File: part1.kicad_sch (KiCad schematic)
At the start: 20 parts, among them U1 74LS377, U10 Am2918, U11 Am2919, U12 Am2919, U13 74LS139, U14 74LS399, U15 74LS175, U16 Am2921, U17 Am2921, U18 Am27S19, U19 Am27S19, U2 Am2919, U3 Am2919, U4 Am27S21, U5 Am27S21, U6 Am27S21, U7 Am2910, U8 Am2918, U9 Am2918

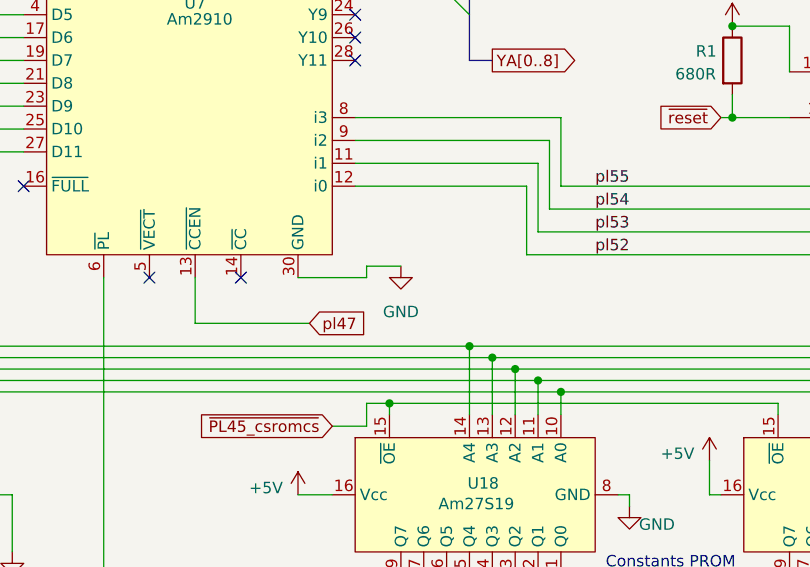
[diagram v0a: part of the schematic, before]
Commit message: Start with ALU sheet
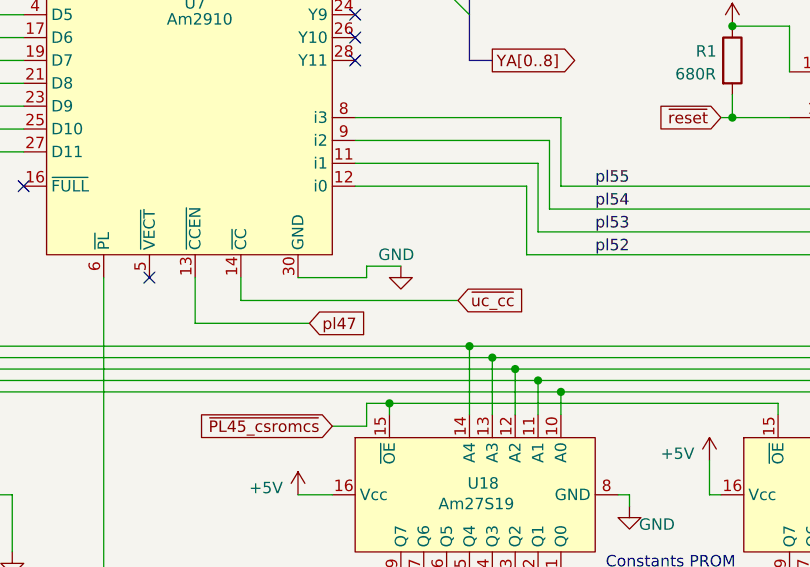
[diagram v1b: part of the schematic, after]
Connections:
- net ~{uc_cc}: now reaches U7.14 (~{CC})
- no-connect marks 28 -> 27
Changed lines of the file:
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@@
 	)
 	(no_connect
-		(at 176.53 153.67)
-	)
-	(no_connect
 		(at 166.37 153.67)
 	)
@@
 	(wire
 		(pts
+			(xy 176.53 156.21) (xy 176.53 153.67)
+		)
+		(stroke
+			(width 0)
+			(type default)
+		)
+	)
+	(wire
+		(pts
 			(xy 339.09 165.1) (xy 341.63 165.1)
 		)
@@
 	(wire
 		(pts
+			(xy 200.66 156.21) (xy 176.53 156.21)
+		)
+		(stroke
+			(width 0)
+			(type default)
+		)
+	)
+	(wire
+		(pts
 			(xy 295.91 151.13) (xy 295.91 166.37)
 		)
@@
 		)
 	)
+	(global_label "~{uc_cc}"
+		(shape input)
+		(at 200.66 156.21 0)
+		(fields_autoplaced yes)
+		(effects
+			(font
+				(size 1.27 1.27)
+			)
+			(justify left)
+		)
+		(property "Intersheetrefs" "${INTERSHEET_REFS}"
+			(at 209.0276 156.21 0)
+			(hide yes)
+			(show_name no)
+			(do_not_autoplace no)
+			(effects
+				(font
+					(size 1.27 1.27)
+				)
+				(justify left)
+			)
+		)
+	)
 	(global_label "alu_a3"
 		(shape output)
@@
 		(in_pos_files yes)
 		(dnp no)
-		(fields_autoplaced yes)
 		(property "Reference" "#PWR016"
 			(at 194.31 158.75 0)
@@
 		)
 		(property "Value" "GND"
-			(at 194.31 157.48 0)
+			(at 193.802 151.13 0)
 			(show_name no)
 			(do_not_autoplace no)

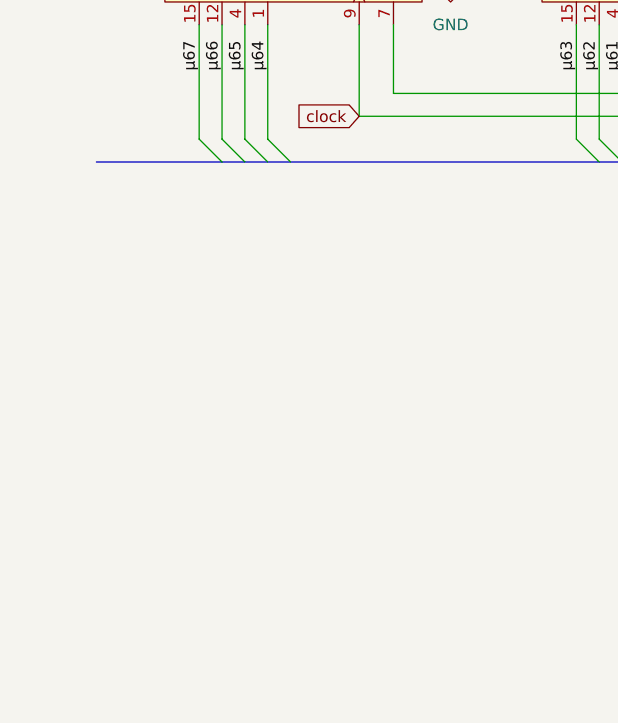
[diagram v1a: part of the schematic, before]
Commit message: More parts of the schema
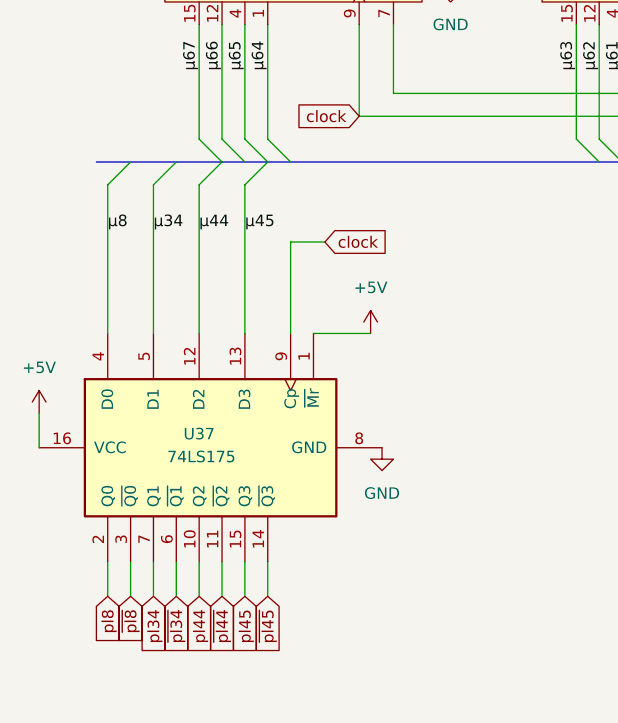
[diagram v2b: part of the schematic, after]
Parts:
- added U37: 74LS175, symbol 74xx:74LS175
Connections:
- net +5V: now also U37.1 (~{Mr}), U37.16 (VCC)
- net GND: now also U37.8 (GND)
- net clock: now also U37.9 (Cp)
- net pl34: now also U37.7 (Q1)
- net pl44: now also U37.10 (Q2)
- net pl45: now also U37.15 (Q3)
- net ~{pl34}: now also U37.6 (~{Q1})
- net ~{pl44}: now also U37.11 (~{Q2})
- new net pl8: U37.2 (Q0)
- new net ~{pl45}: U37.14 (~{Q3})
- new net ~{pl8}: U37.3 (~{Q0})
- new net µ34: U37.5 (D1)
- new net µ44: U37.12 (D2)
- new net µ45: U37.13 (D3)
- new net µ8: U37.4 (D0)
